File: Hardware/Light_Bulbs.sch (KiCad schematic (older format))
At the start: 44 parts, among them J1 DNP, Q1 DMG3414U, Q2 DMG3414U, Q3 DMG3414U, Q4 DMG3414U, U1 PIC18F23K22

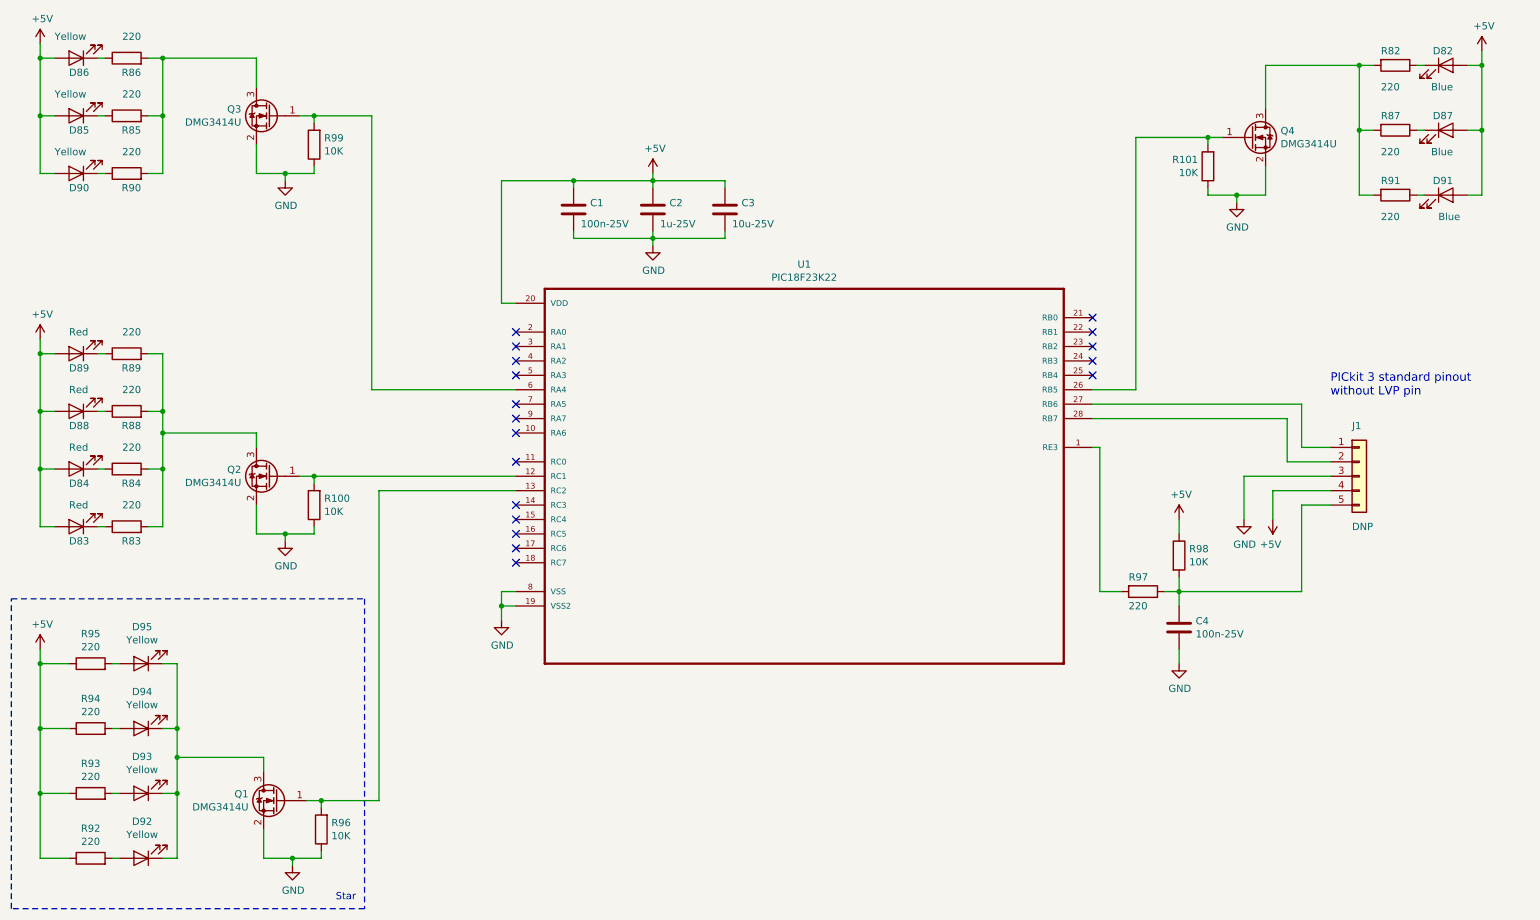
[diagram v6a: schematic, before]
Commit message: Updated bill of materials data on schematic to improve generated bill of materials.
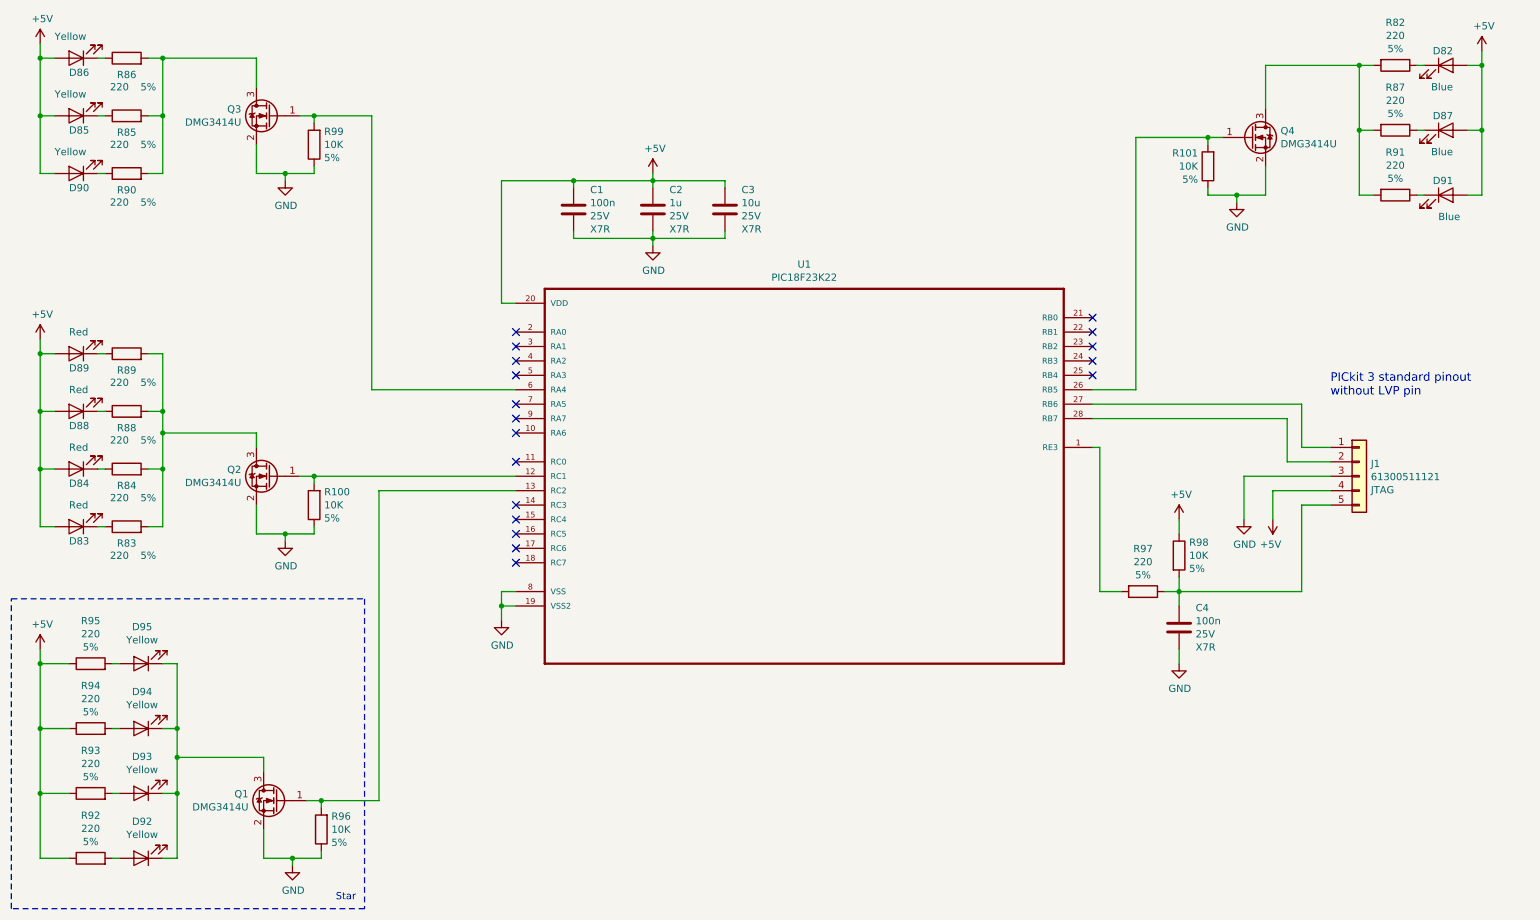
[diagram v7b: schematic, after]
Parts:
- C1, C4: value 100n-25V -> 100n; footprint Capacitor_SMD:C_1206_3216Metric_Pad1.42x1.75mm_HandSolder -> Capacitor_SMD:C_1206_3216Metric_Pad1.33x1.80mm_HandSolder; Value2 (none) -> 25V; Value3 (none) -> X7R
- C2: value 1u-25V -> 1u; footprint Capacitor_SMD:C_1206_3216Metric_Pad1.42x1.75mm_HandSolder -> Capacitor_SMD:C_1206_3216Metric_Pad1.33x1.80mm_HandSolder; Value2 (none) -> 25V; Value3 (none) -> X7R
- C3: value 10u-25V -> 10u; footprint Capacitor_SMD:C_1206_3216Metric_Pad1.42x1.75mm_HandSolder -> Capacitor_SMD:C_1206_3216Metric_Pad1.33x1.80mm_HandSolder; Value2 (none) -> 25V; Value3 (none) -> X7R
- J1: value DNP -> 61300511121; Description (none) -> JTAG; Manufacturer (none) -> Wurth; Populate (none) -> DNP
- R100, R101, R82, R83, R84, R85, R86, R87, R88, R89, R90, R91, R92, R93, R94, R95, R96, R97, R98, R99: Value2 (none) -> 5%
